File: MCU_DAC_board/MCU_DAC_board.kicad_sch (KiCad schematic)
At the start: 75 parts, among them J1 Conn_01x08_Socket, J10 Screw_Terminal_01x02, J2 Conn_01x08_Socket, J3 Conn_01x08_Socket, J4 Conn_01x08_Socket, J5 Barrel_Jack, J6 Barrel_Jack, J7 Screw_Terminal_01x02, J8 Screw_Terminal_01x02, J9 Screw_Terminal_01x02, Q1 FZT953, U1 ADAU1966AWBSTZ, U2 ESP32-WROOM 30-pin dev board

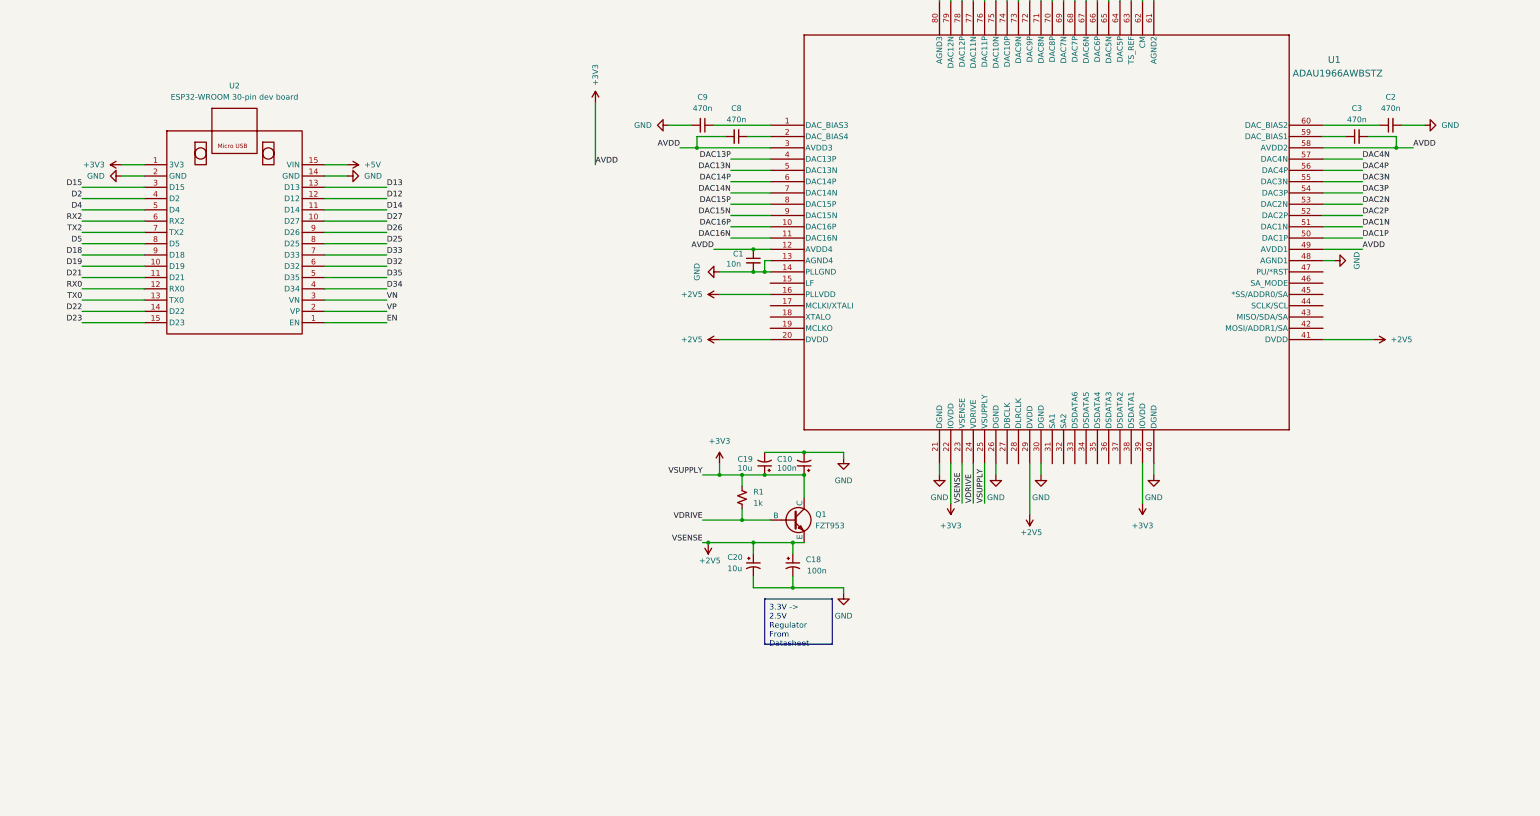
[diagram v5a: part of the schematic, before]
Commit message: Added new MCU board footprint and symbol
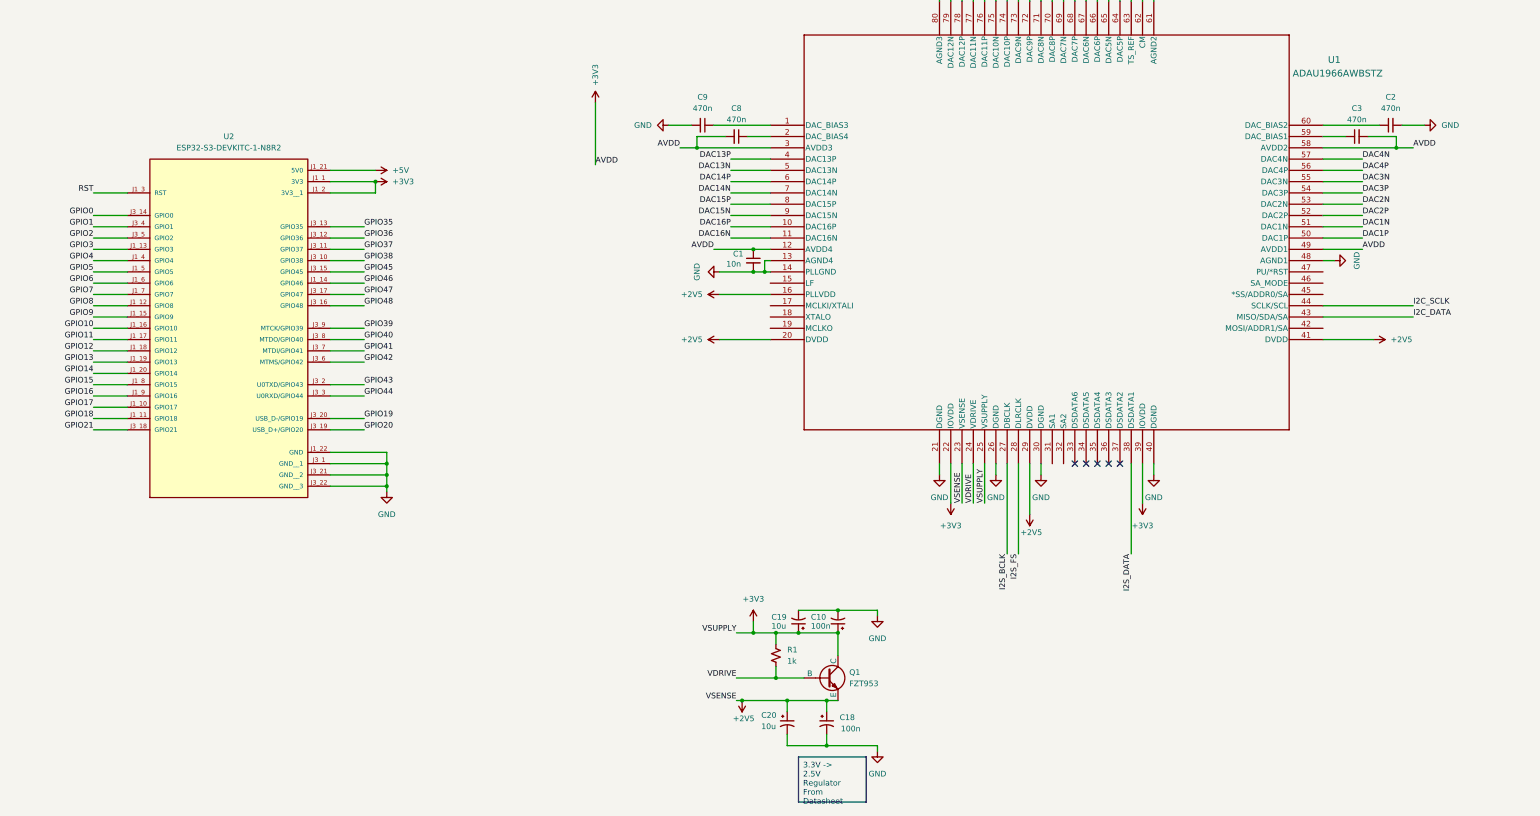
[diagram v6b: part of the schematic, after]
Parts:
- removed U2: ESP32-WROOM 30-pin dev board, project_lib:ESP32-WROOM-30-DEVBOARD, symbol project_lib:ESP32-WROOM 30-pin dev board
- added U2: ESP32-S3-DEVKITC-1-N8R2, ESP32-S3-DEVKITC-1-N8R2:XCVR_ESP32-S3-DEVKITC-1-N8R2, symbol project_lib:ESP32-S3-DEVKITC-1-N8R2
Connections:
- net +3V3: now also U2.J1_1 (3V3), U2.J1_2 (3V3__1)
- net +5V: now also U2.J1_21 (5V0)
- net GND: now also U2.J1_22 (GND), U2.J3_1 (GND__1), U2.J3_21 (GND__2), U2.J3_22 (GND__3)
- net I2S_BCLK: now reaches U1.27 (DBCLK)
- net I2S_FS: now reaches U1.28 (DLRCLK)
- net I2S_DATA: now reaches U1.38 (DSDATA1)
- net I2C_DATA: now reaches U1.43 (MISO/SDA/SA)
- net I2C_SCLK: now reaches U1.44 (SCLK/SCL)
- new net GPIO0: U2.J3_14 (GPIO0)
- new net GPIO1: U2.J3_4 (GPIO1)
- new net GPIO10: U2.J1_16 (GPIO10)
- new net GPIO11: U2.J1_17 (GPIO11)
- new net GPIO12: U2.J1_18 (GPIO12)
- new net GPIO13: U2.J1_19 (GPIO13)
- new net GPIO14: U2.J1_20 (GPIO14)
- new net GPIO15: U2.J1_8 (GPIO15)
- new net GPIO16: U2.J1_9 (GPIO16)
- new net GPIO17: U2.J1_10 (GPIO17)
- new net GPIO18: U2.J1_11 (GPIO18)
- new net GPIO19: U2.J3_20 (USB_D-/GPIO19)
- new net GPIO2: U2.J3_5 (GPIO2)
- new net GPIO20: U2.J3_19 (USB_D+/GPIO20)
- new net GPIO21: U2.J3_18 (GPIO21)
- new net GPIO3: U2.J1_13 (GPIO3)
- new net GPIO35: U2.J3_13 (GPIO35)
- new net GPIO36: U2.J3_12 (GPIO36)
- new net GPIO37: U2.J3_11 (GPIO37)
- new net GPIO38: U2.J3_10 (GPIO38)
- new net GPIO39: U2.J3_9 (MTCK/GPIO39)
- new net GPIO4: U2.J1_4 (GPIO4)
- new net GPIO40: U2.J3_8 (MTDO/GPIO40)
- new net GPIO41: U2.J3_7 (MTDI/GPIO41)
- new net GPIO42: U2.J3_6 (MTMS/GPIO42)
- new net GPIO43: U2.J3_2 (U0TXD/GPIO43)
- new net GPIO44: U2.J3_3 (U0RXD/GPIO44)
- new net GPIO45: U2.J3_15 (GPIO45)
- new net GPIO46: U2.J1_14 (GPIO46)
- new net GPIO47: U2.J3_17 (GPIO47)
- new net GPIO48: U2.J3_16 (GPIO48)
- new net GPIO5: U2.J1_5 (GPIO5)
- new net GPIO6: U2.J1_6 (GPIO6)
- new net GPIO7: U2.J1_7 (GPIO7)
- new net GPIO8: U2.J1_12 (GPIO8)
- new net GPIO9: U2.J1_15 (GPIO9)
- new net RST: U2.J1_3 (RST)
- no-connect marks 0 -> 5
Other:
- moved on the sheet: C10, C18, C19, C20, Q1, R1

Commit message: Schematic almost done on DAC board
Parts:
- removed J1, J2, J3, J4: Conn_01x08_Socket, symbol Connector:Conn_01x08_Socket
- removed J5, J6: Barrel_Jack, symbol Connector:Barrel_Jack
- added C30: 39n, symbol Device:C_Small
- added C31: 2.2n, symbol Device:C_Small
- added J1, J2, J3, J4: LD09S24A4GX00LF, LD09S24A4GX00LF:AMPHENOL_LD09S24A4GX00LF, symbol project_lib:LD09S24A4GX00LF
- added J11, J6: 105-0752-001, CONN_0752-001, symbol project_lib:105-0752-001
- added J5: 54-00127, 54-00127:TENSILITY_54-00127, symbol project_lib:54-00127
- added R34: 3.32k, symbol Device:R_Small_US
- added R35: 10k, symbol Device:R_Small_US
- added TP1, TP2, TP3, TP4, TP5, TP6, TP7, TP8, TP9: TestPoint, symbol Connector:TestPoint
- J10, J7, J8, J9: footprint (none) -> 691137710002:691137710002; symbol Connector:Screw_Terminal_01x02 -> project_lib:691137710002
- U1: footprint ST_80_2_ADI -> project_lib:ST_80_2_ADI
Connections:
- net GPIO7 is gone; now on net DAC_*RST: U2.J1_7 (GPIO7)
- net I2C_DATA is gone; now on net GPIO8: U1.43 (MISO/SDA/SA)
- net I2C_SCLK is gone; now on net GPIO9: U1.44 (SCLK/SCL)
- net I2S_BCLK is gone; now on net GPIO4: U1.27 (DBCLK)
- net I2S_DATA is gone; now on net GPIO6: U1.38 (DSDATA1)
- net I2S_FS is gone; now on net GPIO5: U1.28 (DLRCLK)
- net +24V: now also J6.1, J6.2
- net +2V5: now also C31.2, R34.2
- net +3V3: now also R35.1
- net +5V: now also J5.A
- net GND: now also J1.SH1 (SHIELD), J1.SH2 (SHIELD__1), J11.1, J11.2, J2.SH1 (SHIELD), J2.SH2 (SHIELD__1), J3.SH1 (SHIELD), J3.SH2 (SHIELD__1), J4.SH1 (SHIELD), J4.SH2 (SHIELD__1), J5.B, J5.C
- net GPIO4: now also TP4.1
- net GPIO5: now also TP5.1
- net GPIO6: now also TP7.1
- net GPIO8: now also TP8.1
- net GPIO9: now also TP9.1
- net Out8N: now reaches C21.2, R17.2
- net Out8N: now also J2.9
- net Out3P: now reaches C13.1, R6.2
- net Out3P: now also J1.6
- net Out3N: now reaches C13.2, R7.2
- net Out3N: now also J1.7
- net LF: now reaches U1.15 (LF)
- net LF: now also C30.1, C31.1
- net MCLKI/XTALI: now reaches U1.17 (MCLKI/XTALI)
- net MCLKI/XTALI: now also TP1.1
- net XTALO: now reaches U1.18 (XTALO)
- net XTALO: now also TP2.1
- net MCLKO: now reaches U1.19 (MCLKO)
- net MCLKO: now also TP3.1
- net DAC_*RST: now reaches U1.47 (PU/*RST)
- net DAC_*RST: now also R35.2, TP6.1
- net at C12.1, R4.2: now also J1.3
- net at C12.2, R5.2: now also J1.4
- net Out7P: now reaches C17.1, R14.2
- net Out7P: now also J2.6
- net Out7N: now reaches C17.2, R15.2
- net Out7N: now also J2.7
- net at C22.1, R18.2: now also J3.1
- net at C22.2, R19.2: now also J3.2
- net at C11.2, R3.2: now also J1.2
- net at C26.1, R26.2: now also J4.1
- net at C26.2, R27.2: now also J4.2
- net at C27.1, R28.2: now also J4.3
- net at C27.2, R29.2: now also J4.4
- net Out15P: now reaches C28.1, R30.2
- net Out15P: now also J4.6
- net Out15N: now reaches C28.2, R31.2
- net Out15N: now also J4.7
- net Out16P: now reaches C29.1, R32.2
- net Out16P: now also J4.8
- net Out16N: now reaches C29.2, R33.2
- net Out16N: now also J4.9
- net Out12P: now reaches C25.1, R24.2
- net Out12P: now also J3.8
- net Out12N: now reaches C25.2, R25.2
- net Out12N: now also J3.9
- net Out11P: now reaches C24.1, R22.2
- net Out11P: now also J3.6
- net Out8P: now reaches C21.1, R16.2
- net Out8P: now also J2.8
- net Out11N: now reaches C24.2, R23.2
- net Out11N: now also J3.7
- net at C16.1, R12.2: now also J2.3
- net at C11.1, R2.2: now also J1.1
- net Out4P: now reaches C14.1, R8.2
- net Out4P: now also J1.8
- net Out4N: now reaches C14.2, R9.2
- net Out4N: now also J1.9
- net at C23.2, R21.2: now also J3.4
- net at C15.2, R11.2: now also J2.2
- net at C16.2, R13.2: now also J2.4
- net at C15.1, R10.2: now also J2.1
- net at C23.1, R20.2: now also J3.3
- new net: C30.2, R34.1
- no-connect marks 5 -> 15
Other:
- moved on the sheet: J10, J7, J8, J9

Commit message: Started layout of ADAU1966 area
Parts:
- removed C11, C12, C13, C14, C15, C16, C17, C21, C22, C23, C24, C25, C26, C27, C28, C29: 4n, symbol Device:C_Small
- removed J1, J2, J3, J4: LD09S24A4GX00LF, LD09S24A4GX00LF:AMPHENOL_LD09S24A4GX00LF, symbol project_lib:LD09S24A4GX00LF
- removed R10, R11, R12, R13, R14, R15, R16, R17, R18, R19, R2, R20, R21, R22, R23, R24, R25, R26, R27, R28, R29, R3, R30, R31, R32, R33, R4, R5, R6, R7, R8, R9: 500, symbol Device:R_Small_US
- added R36, R37: 2k, Resistor_SMD:R_0805_2012Metric_Pad1.20x1.40mm_HandSolder, symbol Device:R_Small_US
- C1, C10, C18, C19, C2, C20, C3, C30, C31, C4, C5, C6, C7, C8, C9: footprint (none) -> Capacitor_SMD:C_0805_2012Metric_Pad1.18x1.45mm_HandSolder
- J10, J7, J8, J9: footprint 691137710002:691137710002 -> project_lib:691137710002
- J11, J6: footprint CONN_0752-001 -> project_lib:CONN_0752-001
- J5: footprint 54-00127:TENSILITY_54-00127 -> project_lib:TENSILITY_54-00127
- Q1: footprint (none) -> Package_TO_SOT_SMD:SOT-223-3_TabPin2
- R1, R34: footprint (none) -> Resistor_SMD:R_0805_2012Metric_Pad1.20x1.40mm_HandSolder
- R35: value 10k -> 2k; footprint (none) -> Resistor_SMD:R_0805_2012Metric_Pad1.20x1.40mm_HandSolder
- TP1: value TestPoint -> MCLKI/XTALI; footprint (none) -> project_lib:TP_1.8x1mm
- TP2: value TestPoint -> XTALO; footprint (none) -> project_lib:TP_1.8x1mm
- TP3: value TestPoint -> MCLKO; footprint (none) -> project_lib:TP_1.8x1mm
- TP4: value TestPoint -> I2S_BCLK; footprint (none) -> project_lib:TP_1.8x1mm
- TP5: value TestPoint -> I2S_FS; footprint (none) -> project_lib:TP_1.8x1mm
- TP6: value TestPoint -> DAC_*RST; footprint (none) -> project_lib:TP_1.8x1mm
- TP7: value TestPoint -> I2S_DATA; footprint (none) -> project_lib:TP_1.8x1mm
- TP8: value TestPoint -> I2C_SDA; footprint (none) -> project_lib:TP_1.8x1mm
- TP9: value TestPoint -> I2C_SCL; footprint (none) -> project_lib:TP_1.8x1mm
- U2: footprint ESP32-S3-DEVKITC-1-N8R2:XCVR_ESP32-S3-DEVKITC-1-N8R2 -> project_lib:XCVR_ESP32-S3-DEVKITC-1-N8R2
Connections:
- net +3V3: now also R36.1, R37.1
- net DAC_*RST: now also R36.2; no longer R35.2
- net GND: now also U1.42 (MOSI/ADDR1/SA), U1.45 (*SS/ADDR0/SA)
- net GPIO8: now also R35.2
- net GPIO9: now also R37.2
- no-connect marks 15 -> 6
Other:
- added sheet DAC_filter (dac_filter.kicad_sch)
- added sheet DAC_filter1 (dac_filter.kicad_sch)
- added sheet DAC_filter2 (dac_filter.kicad_sch)
- added sheet DAC_filter3 (dac_filter.kicad_sch)
